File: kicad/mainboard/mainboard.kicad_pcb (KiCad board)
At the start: 2 copper layers, 190.5 x 66 mm, 146 parts, among them J1 +12V BATTERY, J11 Conn_02x12, J12 Conn 02x03, J2 REMOTE INPUT, J3 LINK INPUT, J4 MIC INPUT, J5 LINE INPUT, J6 OUTPUT A, J7 OUTPUT B, J8 VDC INPUT, J9 RADIO INTERFACE, T1 IRL520N, T2 IRL520N, T3 IRF9Z24, T4 IRL520N, T5 IRL520N, T6 IRF9Z24, U1 ATMEGA16/32-P, U10 LM358N, U11 7809TV, U12 7809TV, U13 7805TV, U14 LM2941T, U2 LM324N, U4 LM358N, U8 LTC1661, U9 MAX232

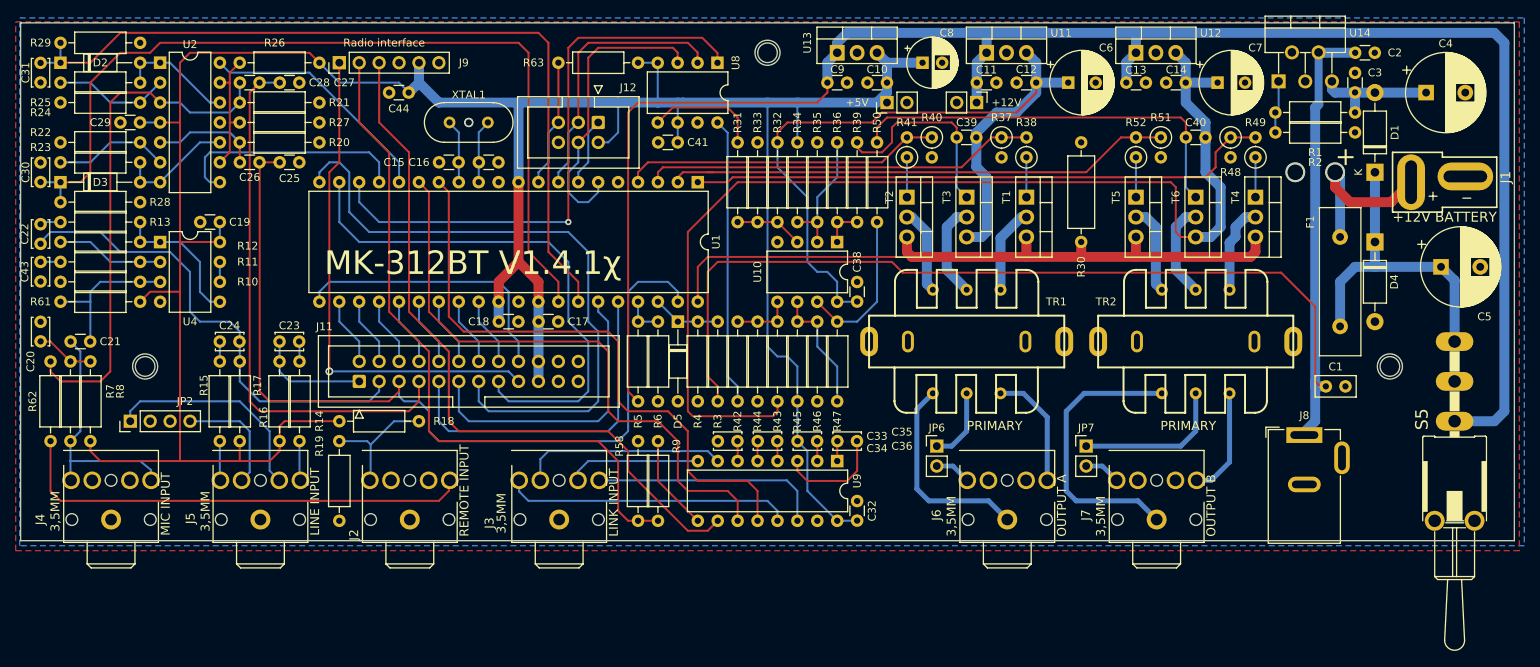
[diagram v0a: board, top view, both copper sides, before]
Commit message: Increase clearance around primary side of transformers. Moved name and version to a visible spot on the PCB silkscreen.
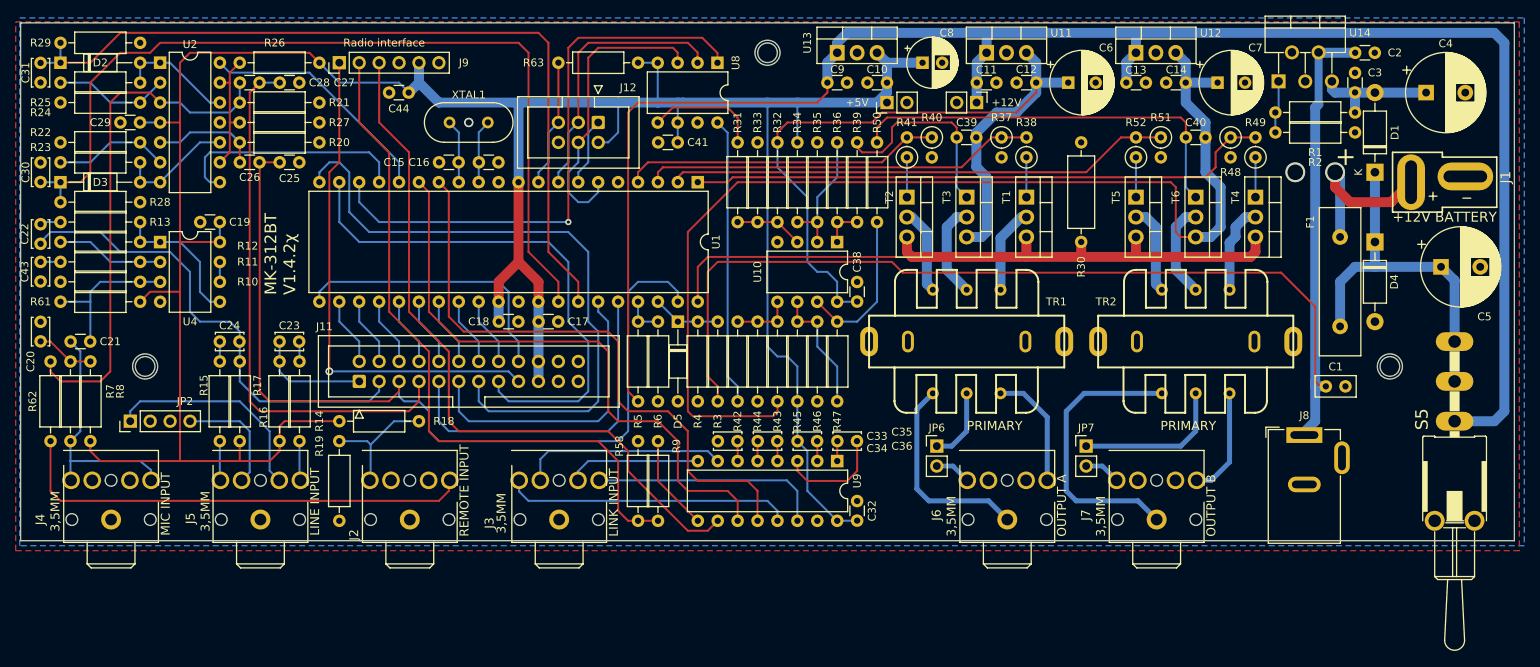
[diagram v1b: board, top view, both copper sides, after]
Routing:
- net PB1: track 65.0 -> 63.7 mm
- net Net-(C39-Pad1): track 26.0 -> 25.3 mm
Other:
- board text added: "MK-312BT V1.4.2χ"
- board text removed: "MK-312BT V1.4.1χ"
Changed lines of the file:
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@@
   (title_block
     (title "MK312-BT Mainboard")
-    (date "2022-09-04")
-    (rev "1.4.1-Chi")
+    (date "2022-12-29")
+    (rev "1.4.2-Chi")
   )
   (layers
@@
     (effects (font (size 2.3368 2.3368) (thickness 0.2032)) (justify left bottom))
   )
-  (gr_text "MK-312BT V1.4.1χ" (at 89.535 83.185) (layer "F.SilkS")
-    (effects (font (size 3 3) (thickness 0.381)) (justify left bottom))
+  (gr_text "MK-312BT\nV1.4.2χ" (at 86 85.5 90) (layer "F.SilkS")
+    (effects (font (size 1.5 1.5) (thickness 0.3)) (justify left bottom))
   )
   (gr_text "PRIMARY" (at 196.153369 102.87) (layer "F.SilkS")
@@
   (segment (start 161.925 81.28) (end 139.7 81.28) (width 0.254) (layer "F.Cu") (net 1))
   (segment (start 138.43 95.885) (end 139.7 97.155) (width 0.254) (layer "F.Cu") (net 1))
-  (segment (start 163.2948 82.6498) (end 162.56 81.915) (width 0.254) (layer "F.Cu") (net 1))
+  (segment (start 161.925 81.28) (end 163.2948 82.6498) (width 0.254) (layer "F.Cu") (net 1))
   (segment (start 215.9 86.995) (end 215.9 96.52) (width 0.254) (layer "F.Cu") (net 1))
-  (segment (start 162.56 81.915) (end 161.925 81.28) (width 0.254) (layer "F.Cu") (net 1))
   (segment (start 217.257621 97.155) (end 216.535 97.155) (width 0.25) (layer "F.Cu") (net 1))
-  (segment (start 165.0002 82.6498) (end 163.2948 82.6498) (width 0.254) (layer "F.Cu") (net 1))
+  (segment (start 163.2948 82.6498) (end 211.5548 82.6498) (width 0.254) (layer "F.Cu") (net 1))
   (segment (start 139.7 81.28) (end 138.43 82.55) (width 0.254) (layer "F.Cu") (net 1))
   (segment (start 215.9 86.995) (end 211.5548 82.6498) (width 0.254) (layer "F.Cu") (net 1))
-  (segment (start 138.43 83.185) (end 138.43 95.885) (width 0.254) (layer "F.Cu") (net 1))
-  (segment (start 138.43 82.55) (end 138.43 83.185) (width 0.254) (layer "F.Cu") (net 1))
-  (segment (start 211.5548 82.6498) (end 165.0002 82.6498) (width 0.254) (layer "F.Cu") (net 1))
+  (segment (start 138.43 82.55) (end 138.43 95.885) (width 0.254) (layer "F.Cu") (net 1))
   (segment (start 139.7 97.155) (end 139.7 99.06) (width 0.254) (layer "F.Cu") (net 1))
   (segment (start 216.535 97.155) (end 215.9 96.52) (width 0.25) (layer "F.Cu") (net 1))
@@
   (segment (start 172.74 58.42) (end 172.74 55.86) (width 1.27) (layer "B.Cu") (net 3))
   (segment (start 153.69 58.42) (end 153.69 55.86) (width 1.27) (layer "B.Cu") (net 3))
-  (segment (start 172.72 58.44) (end 172.74 58.42) (width 1.27) (layer "B.Cu") (net 3))
   (segment (start 238.76 52.07) (end 193.04 52.07) (width 1.27) (layer "B.Cu") (net 3))
   (segment (start 233.68 101.6) (end 238.76 101.6) (width 1.27) (layer "B.Cu") (net 3))
@@
   (segment (start 170.815 69.215) (end 132.715 69.215) (width 0.254) (layer "F.Cu") (net 9))
   (segment (start 179.07 65.405) (end 175.895 65.405) (width 0.254) (layer "F.Cu") (net 9))
-  (segment (start 139.065 69.85) (end 138.43 69.85) (width 0.254) (layer "F.Cu") (net 10))
   (segment (start 134.62 70.485) (end 135.255 69.85) (width 0.254) (layer "F.Cu") (net 10))
-  (segment (start 135.255 69.85) (end 139.065 69.85) (width 0.254) (layer "F.Cu") (net 10))
   (segment (start 186.69 69.85) (end 191.135 65.405) (width 0.254) (layer "F.Cu") (net 10))
-  (segment (start 139.065 69.85) (end 186.69 69.85) (width 0.254) (layer "F.Cu") (net 10))
-  (segment (start 134.62 71.11) (end 134.62 70.485) (width 0.254) (layer "F.Cu") (net 10))
-  (segment (start 134.615 71.115) (end 134.62 71.11) (width 0.254) (layer "F.Cu") (net 10))
+  (segment (start 135.255 69.85) (end 186.69 69.85) (width 0.254) (layer "F.Cu") (net 10))
   (segment (start 193.04 65.405) (end 196.215 65.405) (width 0.254) (layer "F.Cu") (net 10))
   (segment (start 191.135 65.405) (end 193.04 65.405) (width 0.254) (layer "F.Cu") (net 10))
@@
   (segment (start 101.6 58.42) (end 101.6 55.88) (width 1.27) (layer "B.Cu") (net 21))
   (segment (start 154.94 114.3) (end 151.13 110.49) (width 0.254) (layer "B.Cu") (net 21))
-  (segment (start 132.04 55.88) (end 132.05 55.89) (width 0.254) (layer "B.Cu") (net 21))
   (segment (start 129.54 55.88) (end 132.04 55.88) (width 0.254) (layer "B.Cu") (net 21))
-  (segment (start 149.86 104.12) (end 149.88 104.14) (width 0.254) (layer "B.Cu") (net 21))
   (segment (start 124.46 66.04) (end 125.73 66.04) (width 0.254) (layer "B.Cu") (net 21))
   (segment (start 116.84 93.98) (end 116.84 88.9) (width 1.27) (layer "B.Cu") (net 21))
@@
   (segment (start 173.99 70.485) (end 173.6725 70.1675) (width 1.27) (layer "B.Cu") (net 35))
   (segment (start 172.68 65.405) (end 172.68 64.81) (width 1.27) (layer "B.Cu") (net 35))
-  (segment (start 180.32 55.86) (end 179.07 54.61) (width 1.27) (layer "B.Cu") (net 35))
+  (segment (start 179.07 54.61) (end 180.32 55.86) (width 1.27) (layer "B.Cu") (net 35))
   (segment (start 172.68 69.175) (end 173.6725 70.1675) (width 1.27) (layer "B.Cu") (net 35))
   (segment (start 151.13 81.28) (end 152.4 82.55) (width 0.254) (layer "B.Cu") (net 35))
@@
   (segment (start 154.93 86.37) (end 157.45 86.37) (width 0.254) (layer "B.Cu") (net 35))
   (segment (start 172.68 64.81) (end 175.26 62.23) (width 1.27) (layer "B.Cu") (net 35))
-  (segment (start 157.45 86.37) (end 157.48 86.34) (width 0.254) (layer "B.Cu") (net 35))
   (segment (start 153.67 82.55) (end 154.93 83.81) (width 0.254) (layer "B.Cu") (net 35))
   (segment (start 173.355 78.105) (end 173.99 77.47) (width 1.27) (layer "B.Cu") (net 35))
@@
   (segment (start 172.68 65.405) (end 172.68 69.175) (width 1.27) (layer "B.Cu") (net 35))
   (segment (start 175.26 62.23) (end 177.8 62.23) (width 1.27) (layer "B.Cu") (net 35))
-  (segment (start 180.34 55.88) (end 180.32 55.86) (width 1.27) (layer "B.Cu") (net 35))
   (segment (start 197.485 71.12) (end 142.24 71.12) (width 0.25) (layer "F.Cu") (net 36))
   (segment (start 142.24 71.12) (end 135.89 77.47) (width 0.25) (layer "F.Cu") (net 36))
@@
   (segment (start 169.545 63.5) (end 170.18 64.135) (width 0.254) (layer "F.Cu") (net 44))
   (segment (start 160.655 67.31) (end 161.925 66.04) (width 0.254) (layer "F.Cu") (net 44))
-  (segment (start 157.48 66.04) (end 157.48 66.675) (width 0.254) (layer "F.Cu") (net 44))
   (segment (start 162.56 63.5) (end 169.545 63.5) (width 0.254) (layer "F.Cu") (net 44))
   (segment (start 170.18 64.135) (end 170.18 65.405) (width 0.254) (layer "F.Cu") (net 44))
@@
   (segment (start 168.91 76.835) (end 168.91 82.296) (width 1.27) (layer "B.Cu") (net 52))
   (segment (start 142.24 76.2) (end 147.32 76.2) (width 0.254) (layer "F.Cu") (net 53))
-  (segment (start 147.31 76.21) (end 147.32 76.2) (width 0.254) (layer "F.Cu") (net 53))
-  (segment (start 149.85 78.73) (end 149.85 78.75) (width 0.254) (layer "F.Cu") (net 53))
   (segment (start 147.32 76.2) (end 149.85 78.73) (width 0.254) (layer "F.Cu") (net 53))
   (segment (start 69.85 55.88) (end 74.93 60.96) (width 0.254) (layer "B.Cu") (net 54))
@@
   (segment (start 77.47 63.5) (end 78.74 63.5) (width 0.254) (layer "F.Cu") (net 55))
   (segment (start 77.47 58.42) (end 77.47 63.5) (width 0.254) (layer "F.Cu") (net 55))
-  (segment (start 152.4 78.74) (end 152.39 78.75) (width 0.254) (layer "F.Cu") (net 56))
   (segment (start 152.4 76.2) (end 152.4 78.74) (width 0.254) (layer "F.Cu") (net 56))
   (segment (start 149.86 76.2) (end 152.4 76.2) (width 0.254) (layer "F.Cu") (net 56))
-  (segment (start 149.85 76.21) (end 149.86 76.2) (width 0.254) (layer "F.Cu") (net 56))
   (segment (start 154.94 70.485) (end 154.94 66.04) (width 0.254) (layer "B.Cu") (net 56))
   (segment (start 152.4 76.2) (end 152.4 73.025) (width 0.254) (layer "B.Cu") (net 56))
   (segment (start 152.4 73.025) (end 154.94 70.485) (width 0.254) (layer "B.Cu") (net 56))
   (segment (start 163.83 67.945) (end 163.83 73.025) (width 0.254) (layer "B.Cu") (net 57))
-  (segment (start 154.93 76.21) (end 154.94 76.2) (width 0.254) (layer "F.Cu") (net 58))
   (segment (start 157.48 76.2) (end 154.94 76.2) (width 0.254) (layer "F.Cu") (net 58))
   (segment (start 154.93 78.75) (end 154.93 76.21) (width 0.254) (layer "F.Cu") (net 58))
@@
   (segment (start 179.07 67.945) (end 179.07 73.025) (width 0.254) (layer "B.Cu") (net 62))
   (segment (start 147.32 88.9) (end 142.24 88.9) (width 0.254) (layer "F.Cu") (net 63))
-  (segment (start 147.31 88.89) (end 147.32 88.9) (width 0.254) (layer "F.Cu") (net 63))
   (segment (start 147.31 86.37) (end 147.31 88.89) (width 0.254) (layer "F.Cu") (net 63))
-  (segment (start 147.31 88.89) (end 147.32 88.9) (width 0.254) (layer "B.Cu") (net 63))
   (segment (start 149.85 86.37) (end 149.85 88.89) (width 0.254) (layer "F.Cu") (net 64))
-  (segment (start 149.85 88.89) (end 149.86 88.9) (width 0.254) (layer "F.Cu") (net 64))
   (segment (start 152.4 88.9) (end 149.86 88.9) (width 0.254) (layer "F.Cu") (net 64))
-  (segment (start 149.86 86.38) (end 149.85 86.37) (width 0.254) (layer "B.Cu") (net 64))
   (segment (start 152.4 88.9) (end 152.4 92.075) (width 0.254) (layer "B.Cu") (net 64))
   (segment (start 152.4 92.075) (end 154.94 94.615) (width 0.254) (layer "B.Cu") (net 64))
@@
   (segment (start 199.41 65.405) (end 199.41 71.775) (width 0.254) (layer "B.Cu") (net 66))
   (segment (start 199.41 71.775) (end 200.66 73.025) (width 0.254) (layer "B.Cu") (net 66))
-  (segment (start 154.92 88.9) (end 154.94 88.9) (width 0.254) (layer "F.Cu") (net 67))
   (segment (start 152.39 86.37) (end 154.92 88.9) (width 0.254) (layer "F.Cu") (net 67))
   (segment (start 154.94 88.9) (end 157.48 88.9) (width 0.254) (layer "B.Cu") (net 67))
   (segment (start 157.48 88.9) (end 160.02 86.36) (width 0.254) (layer "B.Cu") (net 67))
   (segment (start 160.02 86.36) (end 160.02 76.2) (width 0.254) (layer "B.Cu") (net 67))
-  (segment (start 154.92 88.9) (end 154.94 88.9) (width 0.254) (layer "B.Cu") (net 67))
   (segment (start 208.28 67.945) (end 208.28 73.025) (width 0.254) (layer "B.Cu") (net 68))
   (segment (start 193.04 67.945) (end 193.04 73.025) (width 0.254) (layer "B.Cu") (net 69))
